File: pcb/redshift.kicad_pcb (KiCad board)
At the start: 4 copper layers, 45 x 63.5 mm, 77 parts, among them IC1 LPC5526JEV98, J1 G-Switch GT-USB-7010ASV, J2 C145962, J3 C2935905, J4 Conn_ARM_JTAG_SWD_10, SW1 SW_SP, SW2 SW_SP, SW3 SW_SP, SW4 PTS810, U1 PAW3399DM‐T4QU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

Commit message: Fix small silkscreen error Remove uneccesary AR-Check file
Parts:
- renumbered TP8 to D+, TP9 to D-
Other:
- board text removed: "D+"
- board text removed: "D-"
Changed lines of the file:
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@@
     (property "exclude_from_bom" "")
     (attr exclude_from_pos_files exclude_from_bom)
-    (fp_text reference "TP8" (at 0 1.648) (layer "B.SilkS")
+    (fp_text reference "D+" (at 0 1.648) (layer "B.SilkS")
       (effects (font (size 1 1) (thickness 0.15)) (justify mirror))
     )
@@
     (property "exclude_from_bom" "")
     (attr exclude_from_pos_files exclude_from_bom)
-    (fp_text reference "TP9" (at 0 1.648) (layer "B.SilkS")
+    (fp_text reference "D-" (at 0 1.648) (layer "B.SilkS")
       (effects (font (size 1 1) (thickness 0.15)) (justify mirror))
     )
@@
     (effects (font (size 1 1) (thickness 0.15)) (justify mirror))
   )
-  (gr_text "D+" (at 122.25 71) (layer "B.SilkS")
-    (effects (font (size 1 1) (thickness 0.15)) (justify mirror))
-  )
-  (gr_text "D-" (at 126 71) (layer "B.SilkS")
-    (effects (font (size 1 1) (thickness 0.15)) (justify mirror))
-  )

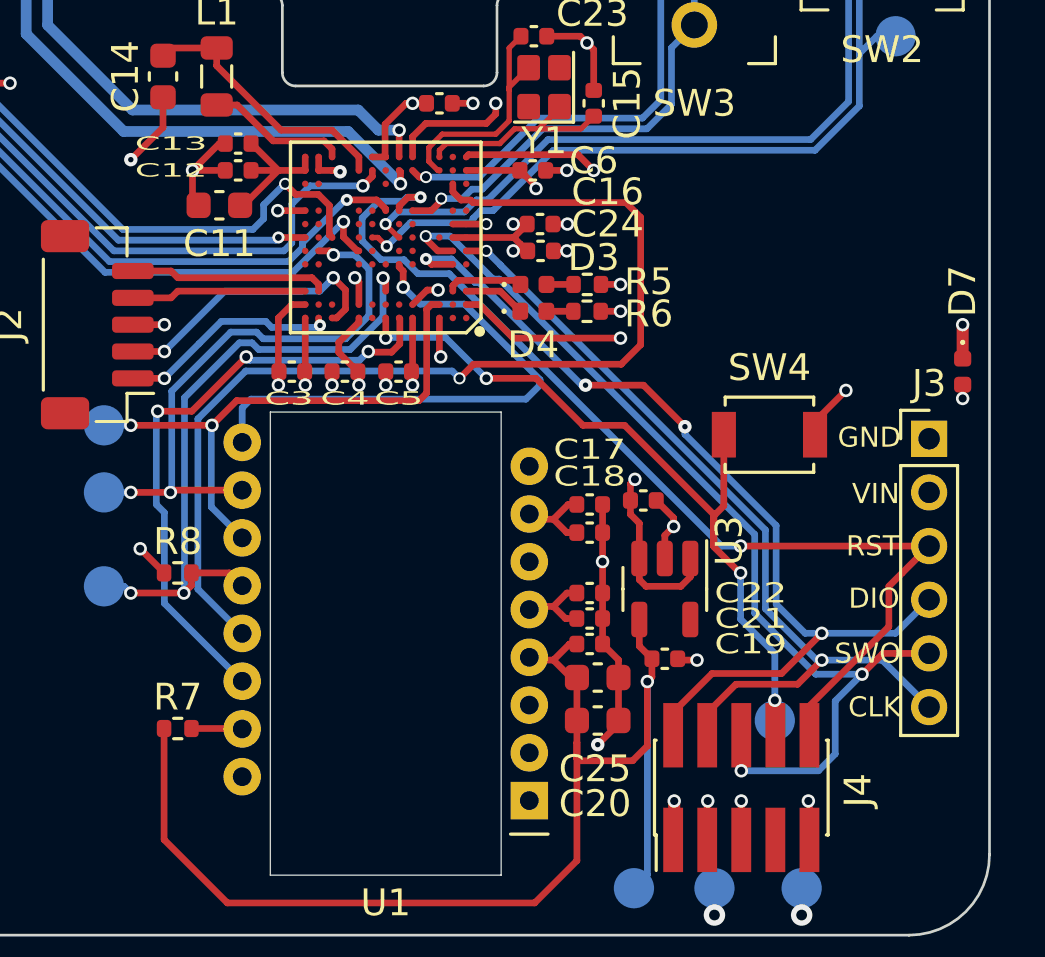
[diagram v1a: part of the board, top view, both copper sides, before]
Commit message: small fixes and updating board from schmatic
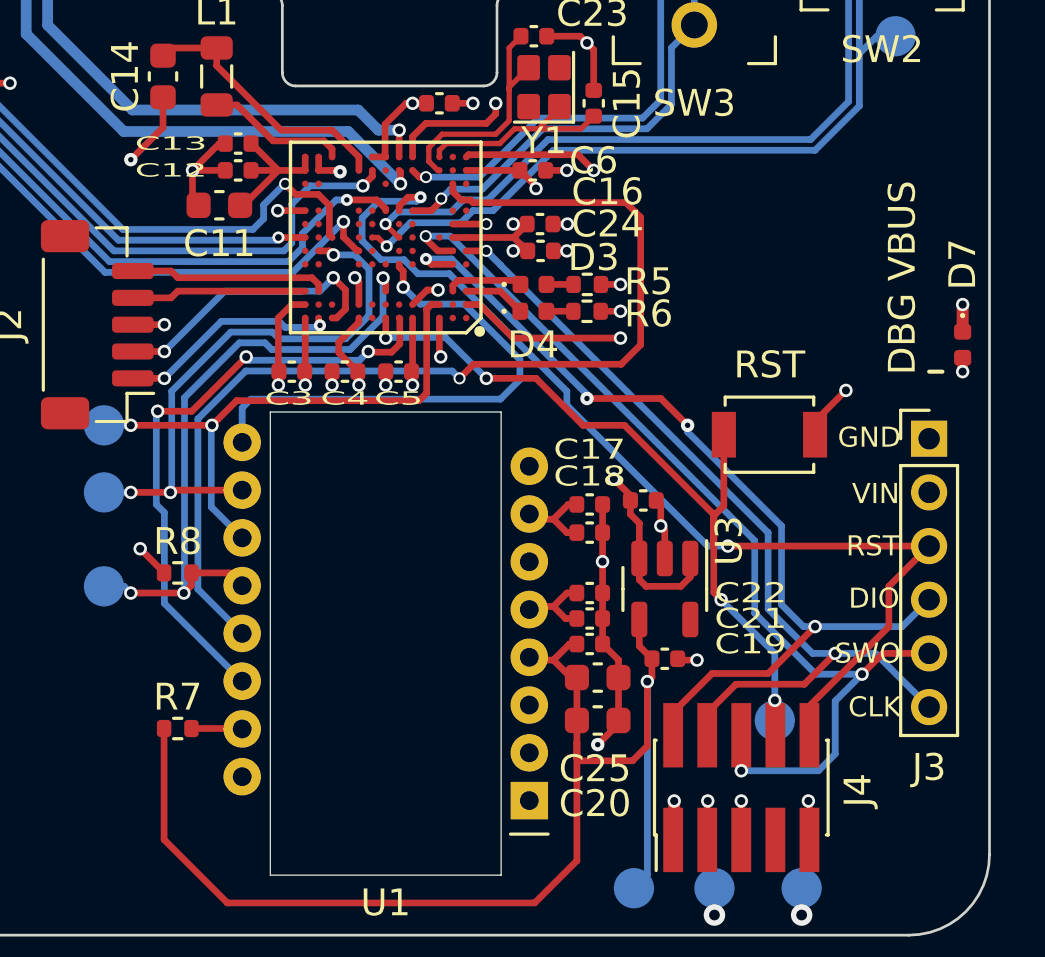
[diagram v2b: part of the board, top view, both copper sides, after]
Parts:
- removed D+, D-: TestPoint, TestPoint:TestPoint_Pad_D1.5mm
- removed kibuzzard-61C38E31: G***, kibuzzard-61C38E31
- removed kibuzzard-622431C0: G***, kibuzzard-622431C0
- added TP8: TestPoint, TestPoint:TestPoint_Pad_D1.5mm, B.Cu at (124.1, 69.8)
- added TP9: TestPoint, TestPoint:TestPoint_Pad_D1.5mm, B.Cu at (129.2, 69.1)
- added kibuzzard-637894B3: G***, kibuzzard-637894B3, B.Cu at (118.2, 92.0)
- added kibuzzard-63789540: G***, kibuzzard-63789540, B.Cu at (118.2, 98.2)
- FB1: value ~ -> 600@100Mhz
- R7: value 13 ±1% -> 13
- moved D7 1.00 mm to (159.0, 97.0)
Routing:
- net /DBG_VIN: track 28.3 -> 30.1 mm
- net /SNSR_MTN: track 20.4 -> 19.2 mm
- net /VBUS_: track 58.7 -> 57.7 mm
- net /SWCLK: track 33.0 -> 33.5 mm
- net +5V: track 59.4 -> 59.9 mm
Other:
- board text added: "Kibuzzard Settings: UbuntuMono-B height 1mm left align"

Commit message: Progress on the PCB routing
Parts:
- removed IC1: LPC5526JEV98, solokeys:BGA98C50P13X13_700X700X97N
- added U4: LPC5528JBD64K, LPC5528JBD64:QFP50P1200X1200X120-65N, F.Cu at (124.5, 93.0)
- moved C24 26.7 mm to (116.6, 91.8), turned to 180 degrees
- moved C6 21.8 mm to (123.8, 100.8), turned to -90 degrees
- moved C16 19.4 mm to (125.8, 100.8), turned to -90 degrees
- moved D2 19.2 mm to (137.9, 94.9), turned to -90 degrees
- moved R4 18.4 mm to (137.9, 96.9), turned to 90 degrees
- moved C4 18.1 mm to (123.2, 85.2), turned to 90 degrees
- moved C23 15.5 mm to (133.6, 97.8)
- moved C5 13.5 mm to (124.8, 100.8), turned to -90 degrees
- moved C15 13.3 mm to (133.6, 94.4), turned to 0 degrees
- moved Y1 13.1 mm to (133.6, 96.1), turned to 180 degrees
- moved J2 12.3 mm to (119.0, 105.8)
- moved C14 8.53 mm to (136.4, 91.5), turned to 0 degrees
- moved R6 8.23 mm to (136.8, 96.9), turned to 90 degrees
- moved C9 7.92 mm to (132.4, 91.5), turned to -90 degrees
- moved C11 7.79 mm to (138.7, 89.3), turned to 0 degrees
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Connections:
- net /FC6_MISO renamed /FC0_MISO
- net /FC6_MOSI renamed /FC0_MOSI
- net /FC6_SCK renamed /FC0_SCK
- U1 pad 13: /FC6_CS1 -> /FC0_CS1
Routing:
- net /FC6_CS1: track 39.0 -> 0.00 mm, vias 1 -> 0
- net /FC0_MISO: track 24.2 -> 0.00 mm, vias 3 -> 0
- net /SNSR_RST: track 22.6 -> 0.00 mm, vias 3 -> 0
- net /FC0_SCK: track 21.6 -> 0.00 mm, vias 3 -> 0
- net /USB1_LED: track 21.5 -> 0.00 mm, vias 2 -> 0
- net /SW1_L_NC: track 28.6 -> 7.55 mm, vias 1 -> 0
- net /FC0_MOSI: track 20.9 -> 0.00 mm, vias 2 -> 0
- net /SW1_L_NO: track 33.3 -> 12.8 mm, vias 1 -> 0
- net /ENC_A: track 36.0 -> 16.3 mm, vias 2 -> 1
- net /SNSR_MTN: track 19.2 -> 0.00 mm, vias 1 -> 0
- net /SWO: track 35.9 -> 17.6 mm, vias 3 -> 2
- net /SW2_R_NC: track 27.4 -> 9.33 mm, vias 1 -> 0
- net /SW2_R_NO: track 32.4 -> 14.5 mm, vias 1 -> 0
- net /ENC_B: track 35.8 -> 18.2 mm, vias 2 -> 1
- net /SWCLK: track 33.5 -> 17.9 mm, vias 2 -> 1
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
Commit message: Routing basically done
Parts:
- moved TP1 2.56 mm to (126.5, 100.5)
- moved TP3 1.98 mm to (127.7, 103.2)
- moved TP5 1.73 mm to (128.2, 107.2)
- moved R8 0.24 mm to (129.9, 105.3)
- moved C3 0.10 mm to (128.3, 100.8)
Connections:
- U4 pad 35: /SW3_M_NC -> /SW2_R_NC
- U4 pad 36: /SW3_M_NO -> /SW2_R_NO
- U4 pad 38: /SW2_R_NC -> /SW3_M_NC
- U4 pad 39: unconnected-(U4-Pad39) -> /SW3_M_NO
- U4 pad 53: /SW2_R_NO -> unconnected-(U4-Pad53)
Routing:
- net /SWCLK: track 17.9 -> 50.4 mm, vias 1 -> 2
- net /ISP: track 16.9 -> 47.5 mm, vias 2 -> 4
- net /SWDIO: track 21.9 -> 50.9 mm, vias 1 -> 2
- net /FC0_SCK: track 0.00 -> 28.5 mm, vias 0 -> 1
- net /SWO: track 17.6 -> 45.8 mm, vias 2 -> 3
- net /SW2_R_NC: track 9.33 -> 36.5 mm, vias 0 -> 1
- net /SW3_M_NC: track 3.78 -> 30.3 mm, vias 0 -> 1
- net /SW2_R_NO: track 14.5 -> 40.4 mm, vias 0 -> 1
- net /FC0_MISO: track 0.00 -> 25.1 mm, vias 0 -> 1
- net /SW3_M_NO: track 10.9 -> 35.4 mm, vias 0 -> 1
- net /FC0_MOSI: track 0.00 -> 23.9 mm, vias 0 -> 1
- net /RESET: track 24.6 -> 43.6 mm, vias 1 -> 2
- net /SNSR_MTN: track 0.00 -> 18.3 mm, vias 0 -> 1
- net /FAULT_LED: track 0.00 -> 18.0 mm, vias 0 -> 2
- net /USB1_LED: track 0.00 -> 17.4 mm, vias 0 -> 2
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
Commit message: Finished routing Finished Silkscreen placement
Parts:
- moved TP12 4.92 mm to (157.4, 115.1)
- moved TP14 3.01 mm to (152.8, 117.0)
- moved TP5 1.64 mm to (126.8, 108.0)
- moved TP3 1.58 mm to (126.2, 103.1)
- moved TP16 0.51 mm to (147.2, 117.2)
- moved TP1 0.31 mm to (126.2, 100.6)
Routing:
- net /1v2: track 5.11 -> 6.86 mm
- net /FC0_MISO: track 25.1 -> 26.7 mm
- net /FC0_MOSI: track 23.9 -> 25.5 mm
- net +3V3: track 39.6 -> 40.7 mm

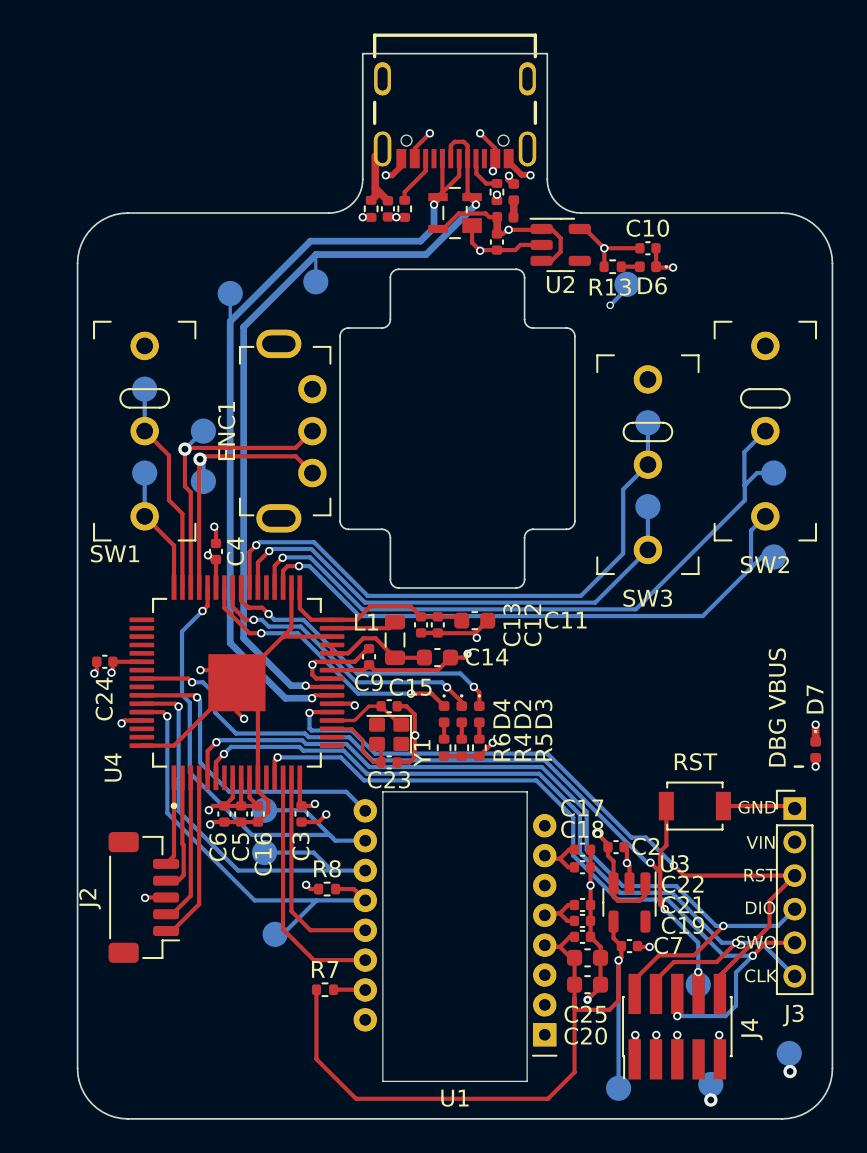
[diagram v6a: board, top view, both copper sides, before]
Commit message: refactor mcu layout for better clarity
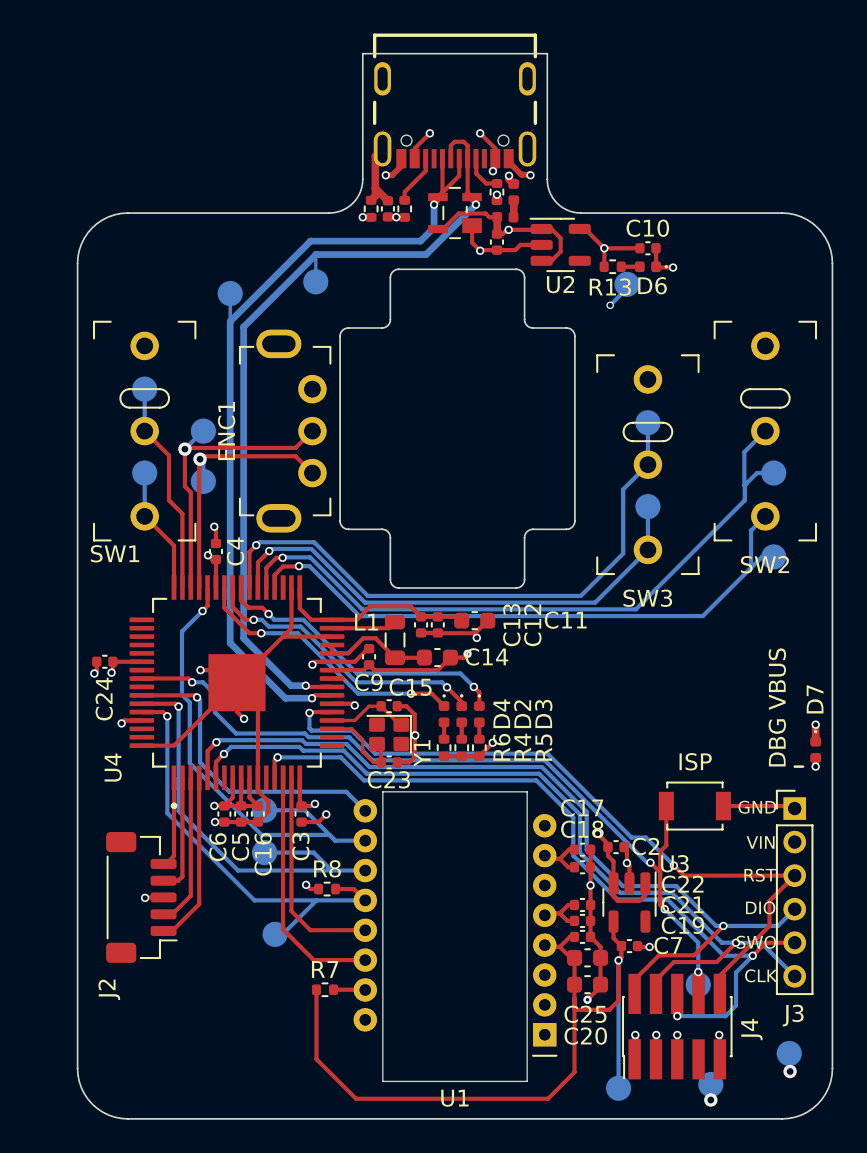
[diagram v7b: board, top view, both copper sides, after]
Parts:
- moved J2 0.15 mm to (118.8, 105.8)
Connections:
- net /PMU renamed /VBAT
- U4 pad 25: +3V3 -> unconnected-(U4-Pad25)
- U4 pad 35: /SW2_R_NC -> unconnected-(U4-Pad35)
- U4 pad 36: /SW2_R_NO -> /SW2_R_NC
- U4 pad 37: unconnected-(U4-Pad37) -> /SW2_R_NO
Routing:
- net +3V3: track 40.7 -> 38.4 mm

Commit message: small fixes, add mounting holes
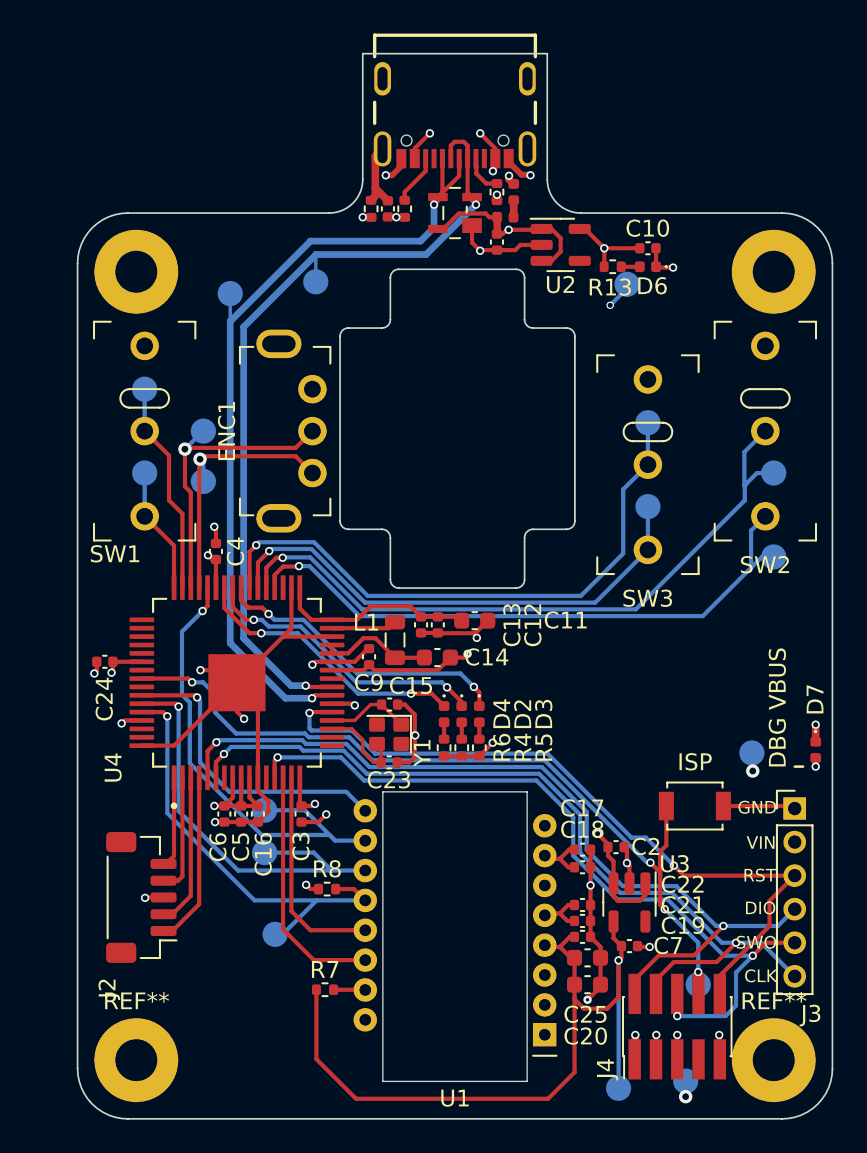
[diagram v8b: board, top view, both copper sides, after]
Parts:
- removed kibuzzard-63789540: G***, kibuzzard-63789540
- added ?: , , F.Cu at (156.5, 68.5)
- added ?: , , F.Cu at (118.5, 68.5)
- added REF**: MountingHole_2.5mm_Pad, MountingHole:MountingHole_2.5mm_Pad, F.Cu at (118.5, 115.5)
- added REF**: MountingHole_2.5mm_Pad, MountingHole:MountingHole_2.5mm_Pad, F.Cu at (156.5, 115.5)
- added kibuzzard-63C8EA46: G***, kibuzzard-63C8EA46, B.Cu at (118.2, 98.2)
- moved TP12 18.1 mm to (155.2, 97.2)
- moved TP14 1.51 mm to (151.2, 116.8)
- moved C15 0.10 mm to (133.6, 94.3)
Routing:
- net +1V9: track 47.3 -> 46.8 mm
